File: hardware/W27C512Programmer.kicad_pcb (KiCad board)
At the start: 2 copper layers, 68.6 x 53.3 mm, 101 parts, among them J1 CTRL, J2 MSB, J3 LSB, J4 Ext_UART, J5 OLED, J6 VP, J7 SAO, Q1 MMBT3904, Q2 MMBT3906, Q3 MMBT3904, Q4 MMBT3904, Q5 MMBT3904, Q6 MMBT3906, Q7 MMBT3906, Q8 MMBT3906, SW1 RST, SW2 USR, U1 MIC2288, U2 74HC573, U3 74HC573, U4 74HC573, U5 28/32 pin ROM

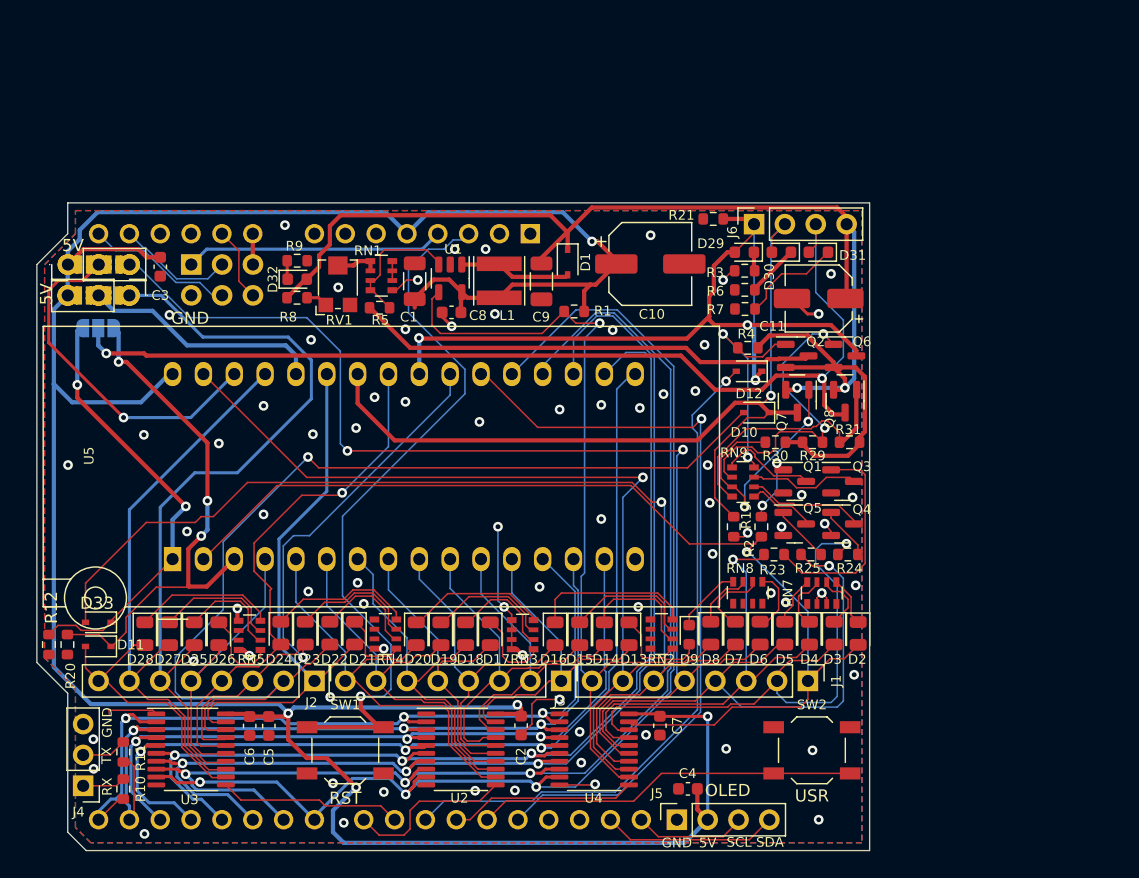
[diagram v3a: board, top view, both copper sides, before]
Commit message: Rev1 PCB - Includes voltage divider on Arduino Analog Pin 2.
Voltage divider on Arduino Analog Pin 2 as well as updated LCSC part numbers.. So you don't end up getting the wrong color LEDs.
Remember to use the Rev1b0 gerber zip file and not Rev0.
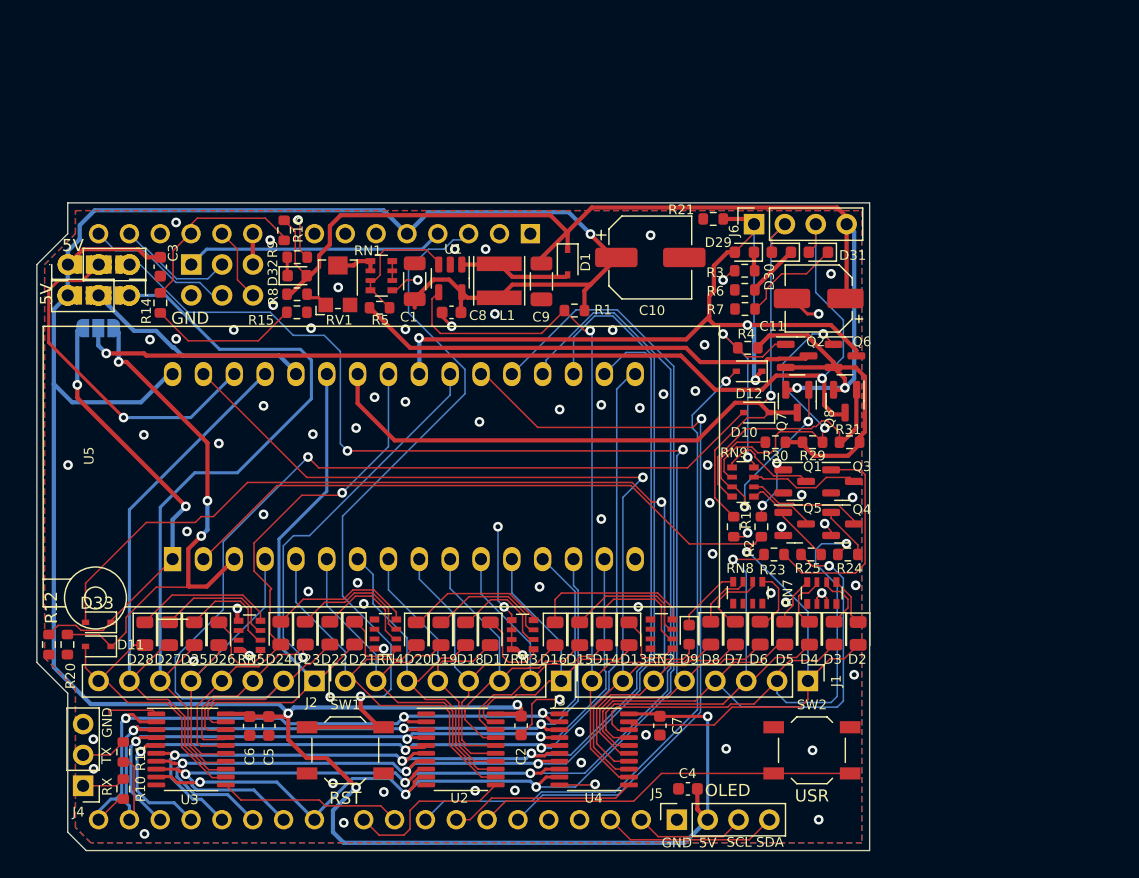
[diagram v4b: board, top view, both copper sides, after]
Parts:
- added R14: 22k, Resistor_SMD:R_0603_1608Metric, F.Cu at (99.7, 55.2)
- added R15: 22k, Resistor_SMD:R_0603_1608Metric, F.Cu at (111.0, 56.0)
- added R16: 270k, Resistor_SMD:R_0603_1608Metric, F.Cu at (109.9, 49.2)
- moved C10 0.53 mm to (140.1, 51.5)
- moved D32 0.29 mm to (111.0, 53.0)
- moved R8 0.29 mm to (111.0, 54.5)
- moved R9 0.29 mm to (111.0, 51.5)
- moved R1 0.08 mm to (133.8, 55.9)
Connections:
- A1 pad 11: unconnected-(A1-Pad11) -> Net-(R16-Pad2)
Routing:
- net Net-(R16-Pad2): track 0.00 -> 15.5 mm
- net Net-(R14-Pad1): track 0.00 -> 12.4 mm
- net VPE: track 112.3 -> 117.8 mm
- net GND: track 39.5 -> 42.9 mm, vias 75 -> 80
- net ~{REG_DISABLE}: track 67.9 -> 65.9 mm
- net /A2: track 28.0 -> 26.8 mm
- net Net-(JP1-Pad2): track 19.7 -> 18.9 mm
- net +5V: track 239.7 -> 240.2 mm
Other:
- board text added: "Relatively Universal ROM Programmer rev 1 ABNielsen.com/65uino"
- board text removed: "Relatively Universal ROM Programmer rev 0 ABNielsen.com/65uino"

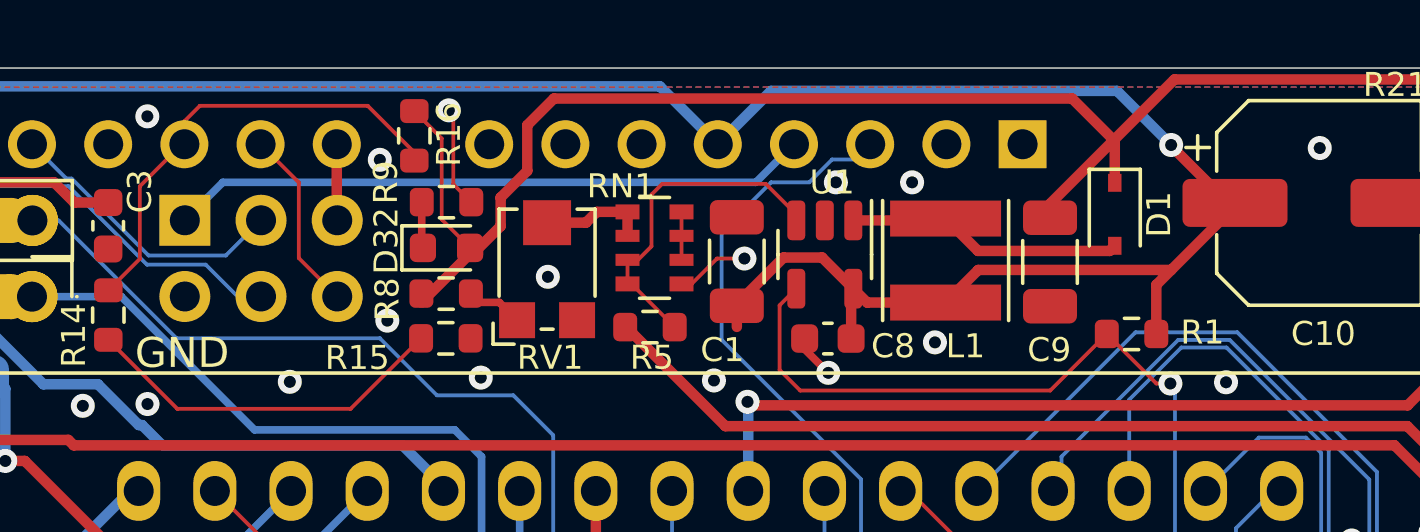
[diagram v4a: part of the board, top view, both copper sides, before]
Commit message: Initial Arduino Firmware Prototype
Arduino sketch that can enable the regulator and has some code to cycle through all addresses.
Uses the Adafruit SSD1306 Library and REV 1 PCB with voltage divider on A2. (270k R1 + 44k R2 if you want to bodge it on Rev0)
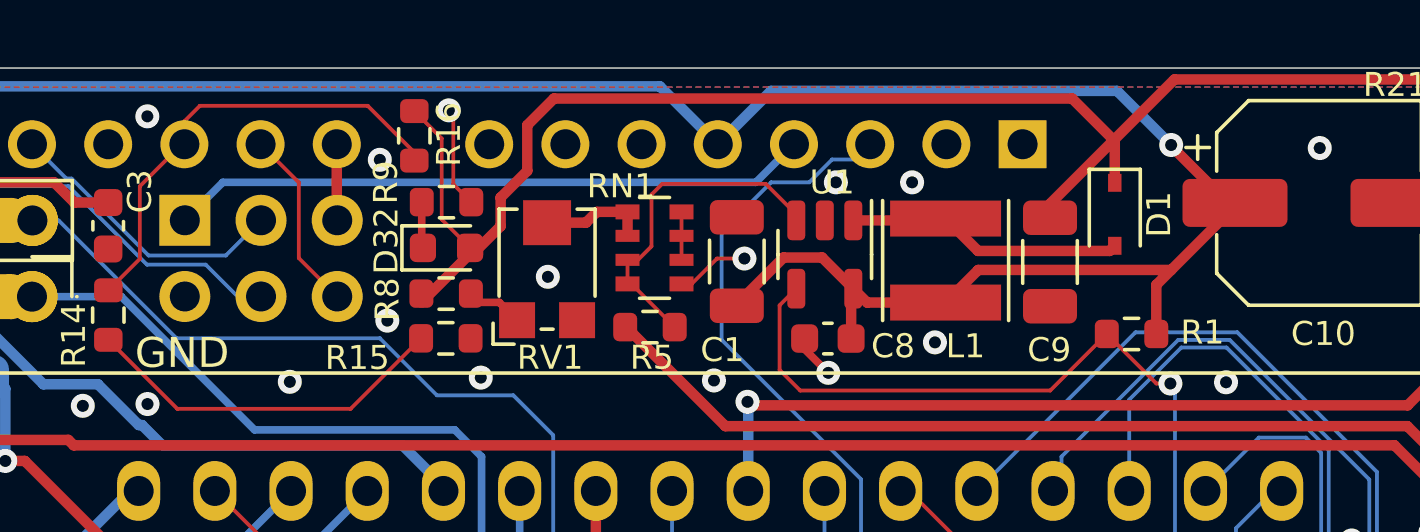
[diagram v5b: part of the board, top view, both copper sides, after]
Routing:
- net +5V: track 240.2 -> 239.4 mm
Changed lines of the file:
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@@
   (segment (start 129.233 89.075) (end 127.3225 89.075) (width 0.35) (layer "F.Cu") (net 4))
   (segment (start 127.6096 54.807) (end 128.6956 53.721) (width 0.35) (layer "F.Cu") (net 4))
-  (segment (start 137.2556 51.5934) (end 137.2556 51.4858) (width 0.35) (layer "F.Cu") (net 4))
   (segment (start 143.9294 95.25) (end 143.9294 96.9394) (width 0.35) (layer "F.Cu") (net 4))
   (segment (start 124.46 56.007) (end 124.46 54.415) (width 0.35) (layer "F.Cu") (net 4))
@@
   (segment (start 107.061 89.2934) (end 108.6358 89.2934) (width 0.35) (layer "F.Cu") (net 4))
   (segment (start 123.4937 53.3063) (end 124.5312 54.3438) (width 0.35) (layer "F.Cu") (net 4))
-  (segment (start 120.65 54.9148) (end 120.65 55.618731) (width 0.35) (layer "F.Cu") (net 4))
   (segment (start 98.5644 51.4728) (end 97.8916 50.8) (width 0.35) (layer "F.Cu") (net 4))
   (segment (start 134.6322 54.2168) (end 135.128 53.721) (width 0.35) (layer "F.Cu") (net 4))
@@
   (segment (start 153.162 58.039) (end 153.162 58.132562) (width 0.35) (layer "F.Cu") (net 14))
   (segment (start 155.9306 62.3824) (end 156.083 62.23) (width 0.35) (layer "F.Cu") (net 14))
-  (segment (start 109.9 48.425) (end 109.9 48.3) (width 0.35) (layer "F.Cu") (net 14))
   (segment (start 156.9568 60.5384) (end 155.1478 60.5384) (width 0.35) (layer "F.Cu") (net 14))
   (segment (start 149.86 57.912) (end 153.035 57.912) (width 0.35) (layer "F.Cu") (net 14))
@@
   (segment (start 109.9 49.8) (end 108.35 48.25) (width 0.127) (layer "F.Cu") (net 112))
   (segment (start 102.75 48.25) (end 102.235 48.765) (width 0.127) (layer "F.Cu") (net 112))
-  (segment (start 102.1525 49.53) (end 102.235 49.53) (width 0.127) (layer "F.Cu") (net 112))
-  (segment (start 109.9 50.075) (end 109.9 49.8) (width 0.127) (layer "F.Cu") (net 112))
   (segment (start 100.75 53.35) (end 100.75 50.9325) (width 0.127) (layer "F.Cu") (net 112))
   (zone (net 5) (net_name "GND") (layer "F.Cu") (hatch edge 0.508)

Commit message: Rev2
Hopefully this does what it's supposed to...
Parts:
- removed JP1: 24pin ROM VCC, Connector_PinHeader_2.54mm:PinHeader_1x03_P2.54mm_Vertical_SolderJumpers
- removed JP2: >=SST39SF020 & 28C512 need A17, Connector_PinHeader_2.54mm:PinHeader_1x03_P2.54mm_Vertical_SolderJumpers
- removed JP3: W27C010/AT27C010 needs p1 VPE/VPP (32 pin), Jumper:SolderJumper-3_P1.3mm_Open_RoundedPad1.0x1.5mm
- removed RN1, RN9: 4k7, Resistor_SMD:R_Array_Convex_4x0603
- added C12: 100nF, Capacitor_SMD:C_0603_1608Metric, F.Cu at (90.4, 55.2)
- added J8: Conn_01x02, Connector_PinHeader_2.54mm:PinHeader_1x02_P2.54mm_Vertical, F.Cu at (139.7, 55.7)
- added JP4: P1_VPP_JMP, Connector_PinHeader_2.54mm:PinHeader_1x02_P2.54mm_Vertical, F.Cu at (90.9, 84.1)
- added JP5: A19_CUT, Jumper:SolderJumper-2_P1.3mm_Bridged_RoundedPad1.0x1.5mm, B.Cu at (98.1, 70.2)
- added Q10: MMBT3906, Package_TO_SOT_SMD:SOT-23, F.Cu at (93.3, 55.4)
- added Q11: MMBT3904, Package_TO_SOT_SMD:SOT-23, F.Cu at (99.0, 55.4)
- added Q12: MMBT3906, Package_TO_SOT_SMD:SOT-23, F.Cu at (93.3, 52.1)
- added Q9: MMBT3904, Package_TO_SOT_SMD:SOT-23, F.Cu at (99.0, 52.1)
- added R13: 4k7, Resistor_SMD:R_0402_1005Metric, F.Cu at (96.2, 53.7)
- added R17: 4k7, Resistor_SMD:R_0402_1005Metric, F.Cu at (96.2, 54.7)
- added R18: 4k7, Resistor_SMD:R_0402_1005Metric, F.Cu at (105.2, 56.4)
- added R22: 4k7, Resistor_SMD:R_0402_1005Metric, F.Cu at (96.2, 55.6)
- added R26: 4k7, Resistor_SMD:R_0402_1005Metric, F.Cu at (96.2, 56.6)
- added R27: 4k7, Resistor_SMD:R_0402_1005Metric, F.Cu at (96.2, 50.9)
- added R28: 4k7, Resistor_SMD:R_0402_1005Metric, F.Cu at (96.2, 51.9)
- added R32: 4k7, Resistor_SMD:R_0402_1005Metric, F.Cu at (96.2, 52.8)
- added R33: 4k7, Resistor_SMD:R_0402_1005Metric, F.Cu at (117.8, 53.3)
- added R34: 4k7, Resistor_SMD:R_0402_1005Metric, F.Cu at (147.6, 68.8)
- added R35: 4k7, Resistor_SMD:R_0402_1005Metric, F.Cu at (117.8, 52.3)
- added R36: 4k7, Resistor_SMD:R_0402_1005Metric, F.Cu at (117.9, 51.3)
- added R37: 4k7, Resistor_SMD:R_0402_1005Metric, F.Cu at (117.9, 54.4)
- added R38: 4k7, Resistor_SMD:R_0402_1005Metric, F.Cu at (147.6, 71.7)
- added R39: 4k7, Resistor_SMD:R_0402_1005Metric, F.Cu at (147.6, 70.8)
- added R40: 4k7, Resistor_SMD:R_0402_1005Metric, F.Cu at (147.6, 69.8)
- added R41: 4k7, Resistor_SMD:R_0402_1005Metric, F.Cu at (90.4, 52.8)
- RN2, RN3, RN4, RN5, RN7, RN8: value 4k7 -> 10k
- moved R14 8.08 mm to (107.7, 56.4), turned to 180 degrees
- moved C3 4.92 mm to (102.4, 56.4), turned to 0 degrees
- moved R12 3.91 mm to (93.0, 86.4), turned to 90 degrees
- moved R20 0.91 mm to (93.0, 83.4)
- moved C10 0.74 mm to (140.1, 50.7)
- moved D11 0.66 mm to (95.2, 83.5)
- moved D33 0.66 mm to (95.2, 81.5)
- moved R19 0.15 mm to (146.9, 73.8)
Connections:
- net ~{RW} renamed P31
- A1 pad 12: unconnected-(A1-Pad12) -> Net-(A1-A3)
- D2 pad 2: A16 -> VPE_TO_VPP
- D33 pad 2: A18 -> P1_VPP_ENABLE
- D7 pad 2: A18 -> A16
- J1 pad 1: A16 -> VPE_TO_VPP
- J1 pad 6: A18 -> A16
- R2 pad 1: A16 -> VPE_TO_VPP
- U4 pad 14: A18 -> A16
- U4 pad 19: A16 -> VPE_TO_VPP
- U5 pad 28: Net-(JP1-Pad2) -> P28
- U5 pad 30: Net-(JP2-Pad2) -> P30
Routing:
- net A18: track 89.7 -> 0.00 mm, vias 1 -> 0
- net P1_VPP_ENABLE: track 46.9 -> 113.8 mm
- net VPE_TO_VPP: track 0.00 -> 35.2 mm, vias 0 -> 1
- net Net-(JP2-Pad2): track 28.6 -> 0.00 mm, vias 1 -> 0
- net Net-(D11-K): track 48.0 -> 22.8 mm, vias 3 -> 0
- net P30: track 0.00 -> 24.6 mm, vias 0 -> 2
- net P28: track 0.00 -> 24.3 mm, vias 0 -> 1
- net Net-(JP1-Pad2): track 18.9 -> 0.00 mm
- net /A13: track 64.6 -> 45.8 mm, vias 0 -> 1
- net GND: track 42.9 -> 57.9 mm, vias 80 -> 88
- net A16: track 87.0 -> 72.0 mm, vias 1 -> 2
- net +5V: track 239.4 -> 253.8 mm, vias 5 -> 8
- net Net-(A1-A3): track 0.00 -> 12.1 mm
- net Net-(R14-Pad1): track 12.4 -> 1.76 mm
- net Net-(Q9-B): track 0.00 -> 9.56 mm
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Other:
- board size 68.6 x 53.3 mm -> 68.8 x 53.6 mm
- board text added: "+5V"
- board text added: "CTRL_LE"
- board text added: "D0"
- board text added: "D1"
- board text added: "D2"
- board text added: "D3"
- board text added: "D4"
- board text added: "D5"
- board text added: "D6"
- board text added: "D7"
- board text added: "JP4: Open for 32 pin ROMs, Closed for 28 pin ROMs (Only for ROMs with VPP on P1)"
- board text added: "JP5: Cut for ROMs with A19 on P1"
- board text added: "P2 / A16"
- board text added: "P32 / ~{RW}"
- board text added: "RLSBLE"
- board text added: "RMSBLE"
- board text added: "Relatively Universal ROM Programmer rev 2 ABNielsen.com/65uino"
- board text added: "USR BTN"
- board text added: "VPE Enable (P24)"
- board text added: "VPE_TO_VPP"
- board text added: "~{CE}"
- board text added: "~{OE}"
- board text added: "~{ROM_CE}"
- board text added: "~{ROM_OE}"
- board text removed: "A"
- board text removed: "A13"
- board text removed: "A18"
- board text removed: "B"
- board text removed: "C"
- board text removed: "D"
- board text removed: "Pins Short on JP1/JP2/JP3 24pin B to 5V 28pin A to 5V, B to A13 32pin B to A13, A to A17* VPP alt Pin1 VPP to C* or D* * = If needed"
- board text removed: "Relatively Universal ROM Programmer rev 1 ABNielsen.com/65uino"
- board text removed: "VPE Enable"
- board text removed: "VPE_TO_VPP / A16"
- board text removed: "VPP"
- board text removed: "~{RW}"

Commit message: Rev2
Untested!
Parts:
- C10: footprint Capacitor_SMD:CP_Elec_6.3x5.4 -> Capacitor_SMD:CP_Elec_6.3x7.7
- C12, C2, C3, C4, C5, C6, C7, C8: footprint Capacitor_SMD:C_0603_1608Metric -> Capacitor_SMD:C_0402_1005Metric
- moved R12 0.51 mm to (92.7, 86.9)
- moved R34 0.36 mm to (147.3, 68.6)
- moved R40 0.32 mm to (147.3, 69.6)
- moved R39 0.30 mm to (147.3, 70.6)
- moved R38 0.25 mm to (147.3, 71.7)
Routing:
- net +5V: track 253.8 -> 257.5 mm
- net VPE_TO_VPP: track 35.2 -> 36.1 mm
- net /A15: track 22.6 -> 23.3 mm
- net VPE: track 117.6 -> 118.2 mm

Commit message: Rev2.1
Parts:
- removed R33: 4k7, Resistor_SMD:R_0402_1005Metric
- added F1: Polyfuse, Fuse:Fuse_0805_2012Metric, F.Cu at (135.4, 53.5)
- added JP6: Bodge point, Jumper:SolderJumper-2_P1.3mm_Bridged_RoundedPad1.0x1.5mm, B.Cu at (119.0, 54.0)
- added JP7: Tin foil socket, Jumper:SolderJumper-2_P1.3mm_Open_RoundedPad1.0x1.5mm, B.Cu at (135.4, 52.7)
- added JP8: Bodge point, Jumper:SolderJumper-2_P1.3mm_Bridged_RoundedPad1.0x1.5mm, B.Cu at (112.0, 54.0)
- added JP9: Bodge point, Jumper:SolderJumper-2_P1.3mm_Bridged_RoundedPad1.0x1.5mm, B.Cu at (119.0, 57.4)
- added R42: 4k7, Resistor_SMD:R_0402_1005Metric, F.Cu at (99.7, 47.9)
- added TP1: TestPoint, TestPoint:TestPoint_Pad_D3.0mm, B.Cu at (115.5, 56.8)
- moved R35 0.76 mm to (117.8, 53.1)
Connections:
- C1 pad 1: +5V -> /5V_REG
- C8 pad 1: +5V -> /5V_REG
- L1 pad 1: +5V -> /5V_REG
- R1 pad 1: +5V -> /5V_REG
- R35 pad 1: Net-(R33-Pad1) -> Net-(R35-Pad1)
- R36 pad 1: Net-(U1-FB) -> /R1E
- R37 pad 1: Net-(U1-FB) -> /Rf2
- R5 pad 2: Net-(U1-FB) -> /FB
- R8 pad 1: VPE -> /R1S
- RV1 pad 2: Net-(R33-Pad1) -> Net-(R35-Pad1)
- RV1 pad 3: unconnected-(RV1-Pad3) -> Net-(R35-Pad1)
- U1 pad 3: Net-(U1-FB) -> /FB
- U1 pad 5: +5V -> /5V_REG
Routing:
- net /5V_REG: track 0.00 -> 23.4 mm, vias 0 -> 1
- net +5V: track 257.5 -> 235.9 mm
- net /FB: track 0.00 -> 11.7 mm, vias 0 -> 1
- net Net-(U1-FB): track 9.32 -> 0.00 mm
- net /Rf2: track 0.00 -> 8.19 mm, vias 0 -> 1
- net Net-(R35-Pad1): track 0.00 -> 6.37 mm
- net Net-(R33-Pad1): track 4.53 -> 0.00 mm
- net /R1S: track 0.00 -> 4.12 mm, vias 0 -> 1
- net /R1E: track 0.00 -> 2.31 mm, vias 0 -> 1
- net D7: track 98.1 -> 100.4 mm
- net VPE: track 118.2 -> 119.7 mm, vias 2 -> 3
- net Net-(A1-A3): track 12.1 -> 13.3 mm
- net SCL2: track 12.2 -> 11.5 mm
- net /A9: track 86.5 -> 85.8 mm
- net /A10: track 46.6 -> 47.3 mm
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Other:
- board text added: "5V_REG"
- board text added: "FB"
- board text added: "R1E"
- board text added: "R1S"
- board text added: "Relatively Universal ROM Programmer rev 2.1 ABNielsen.com/65uino"
- board text added: "Rf2"
- board text removed: "Relatively Universal ROM Programmer rev 2 ABNielsen.com/65uino"
